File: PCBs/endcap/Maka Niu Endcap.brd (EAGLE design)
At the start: 26 x 26 mm, 70 parts, among them J1 U.FL, J2 KELLER_BREAKOUT, J3 GPS_PROG, Q1 20V/0.2A/8MHz/1.2Ω/1Vth, Q2 20V/0.2A/8MHz/1.2Ω/1Vth, U1 P9221-R03MM_PAD, U2 XM1110 GPS, U3 ICM-20948, U4 1.8V/100mA

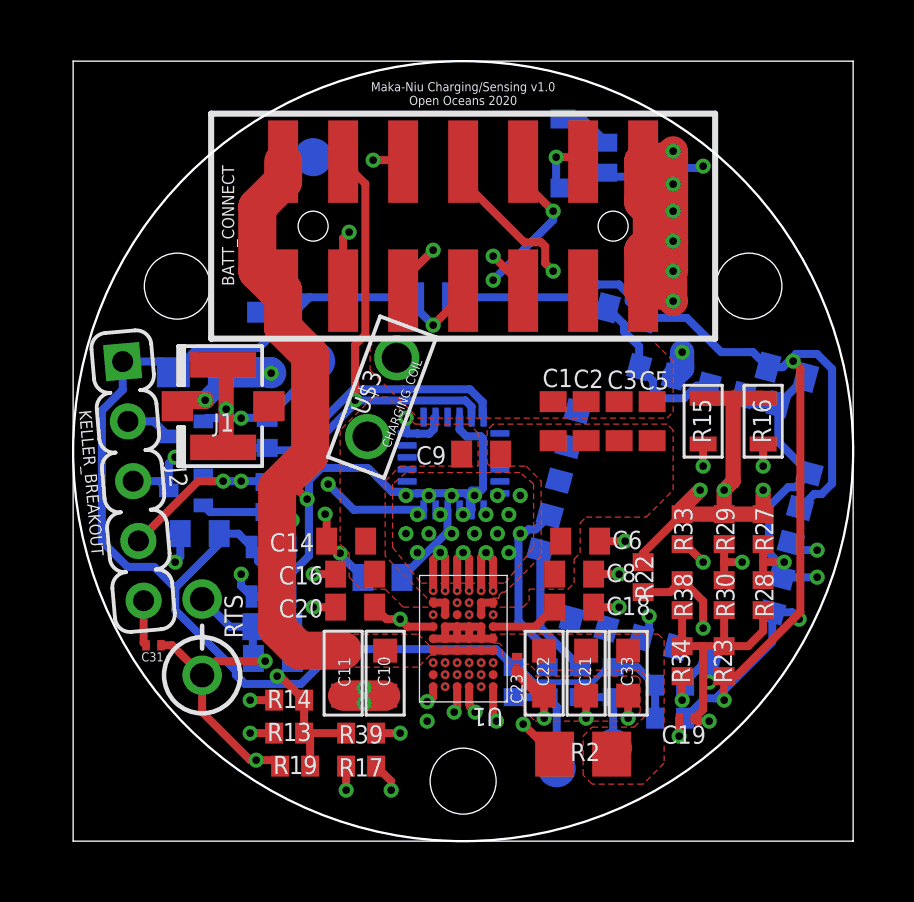
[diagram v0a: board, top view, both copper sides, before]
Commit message: Add files via upload
Silkscreen modified for production
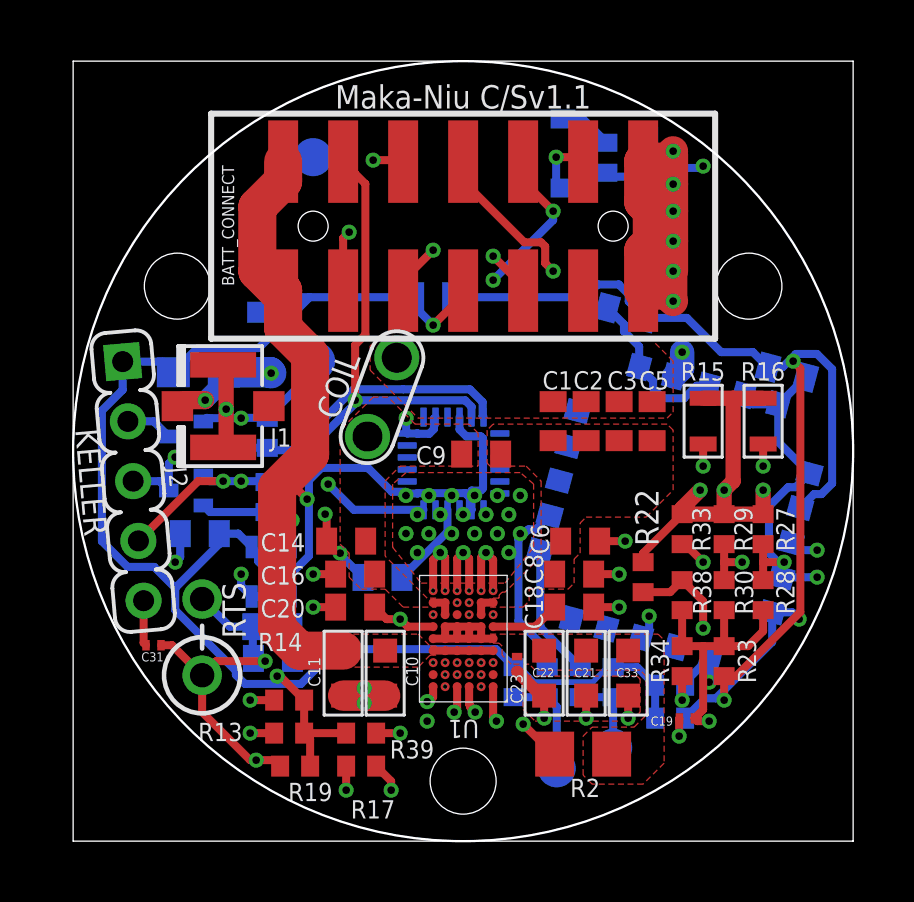
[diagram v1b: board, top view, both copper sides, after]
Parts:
- renumbered U$3 to COIL
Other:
- board text added: "ACC/ GYR"
- board text added: "KELLER"
- board text added: "Maka-Niu C/Sv1.1"
- board text added: "Maka-Niu Charging/ Sensing v1.1 Open Oceans 2021"
- board text removed: "ACC/GYR"
- board text removed: "Maka-Niu Charging/Sensing v1.0 Open Oceans 2020"
